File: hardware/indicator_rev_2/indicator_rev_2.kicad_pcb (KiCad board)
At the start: 2 copper layers, 55 x 56 mm, 28 parts, among them J2 Conn_01x04_Pin, U1 TCA6408ARSVR, U2 TLV70033DCKR

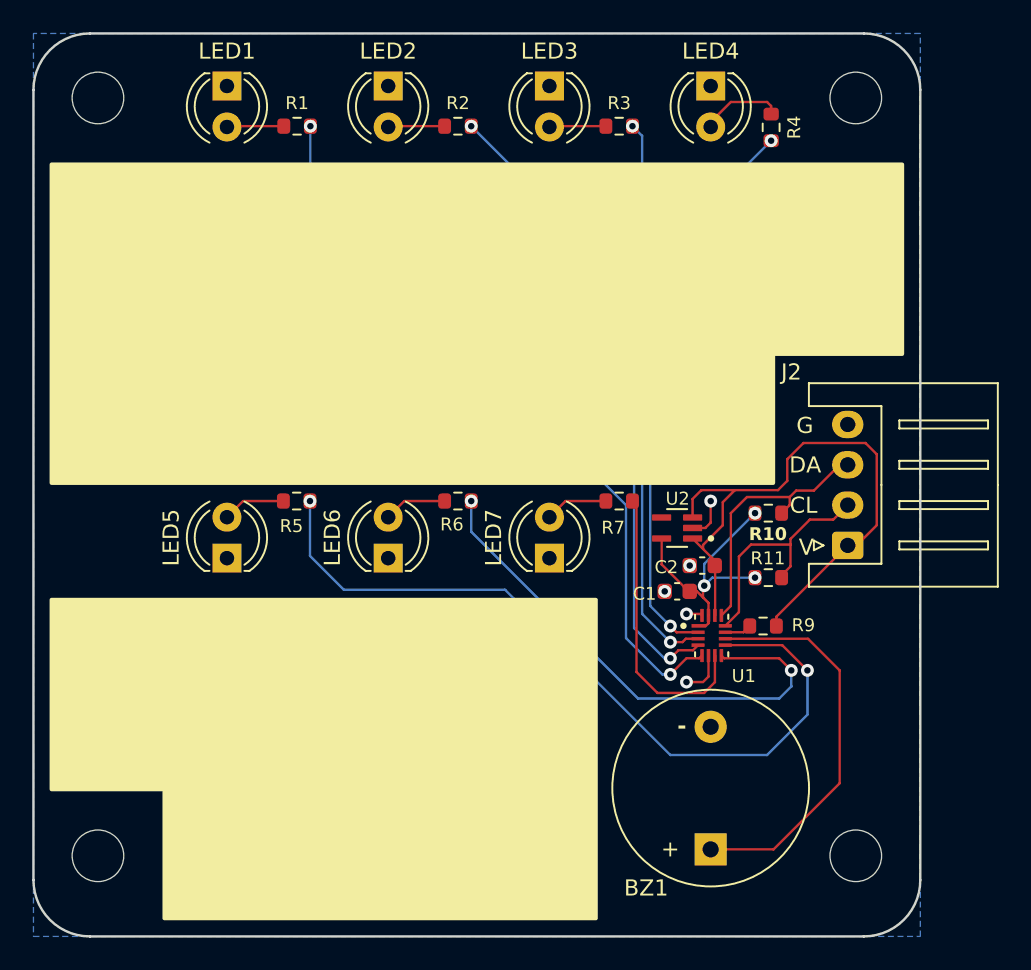
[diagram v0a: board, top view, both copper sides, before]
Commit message: modified i2c header and pushed connector
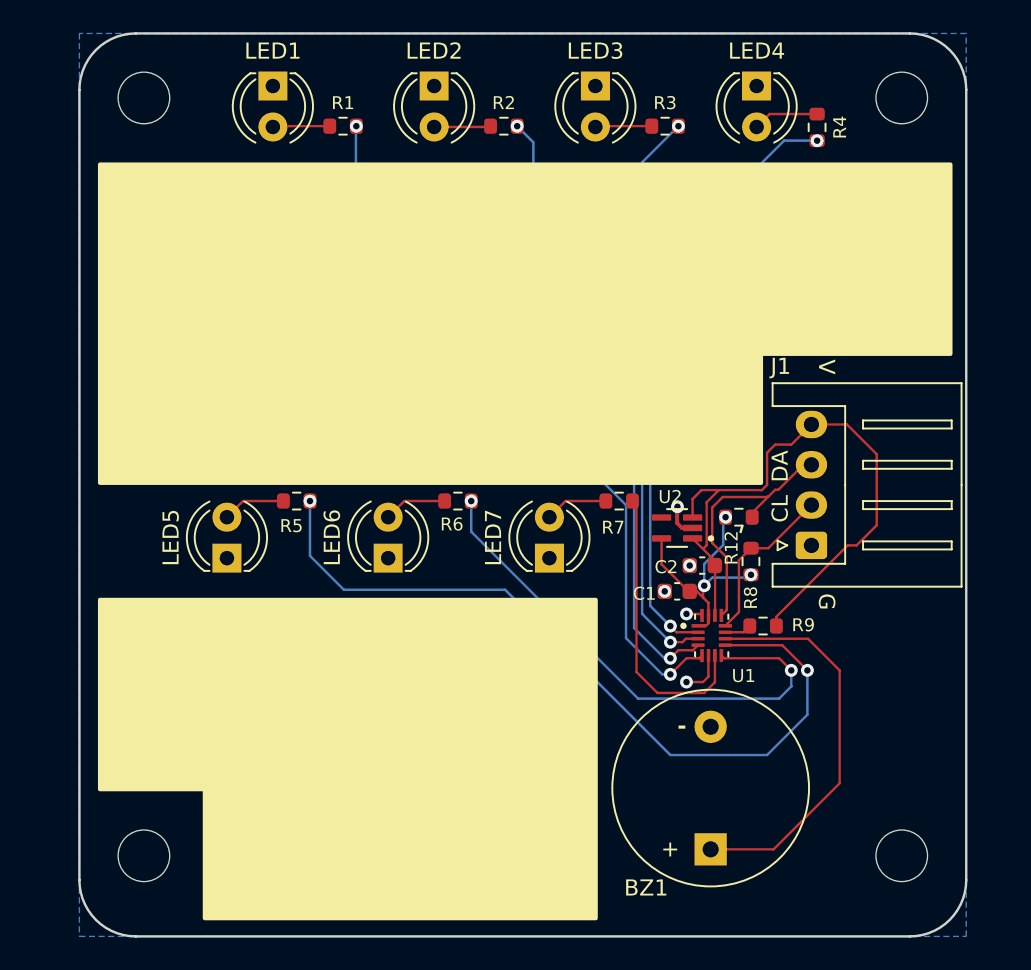
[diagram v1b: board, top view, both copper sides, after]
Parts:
- removed J2: Conn_01x04_Pin, Connector_JST:JST_XH_S4B-XH-A_1x04_P2.50mm_Horizontal
- removed R10, R11: 10k, Resistor_SMD:R_0603_1608Metric
- added J1: Conn_01x04, Connector_JST:JST_XH_S4B-XH-A_1x04_P2.50mm_Horizontal, F.Cu at (147.2, 114.8)
- added R12: 10k, Resistor_SMD:R_0603_1608Metric, F.Cu at (142.8, 113.0)
- added R8: 10k, Resistor_SMD:R_0603_1608Metric, F.Cu at (143.5, 115.8)
- moved R3 2.85 mm to (138.2, 88.8)
- moved R1 2.85 mm to (118.2, 88.8)
- moved R2 2.85 mm to (128.2, 88.8)
- moved LED1 2.85 mm to (113.8, 86.3)
- moved LED2 2.85 mm to (123.8, 86.3)
- moved LED3 2.85 mm to (133.8, 86.3)
- moved LED4 2.85 mm to (143.8, 86.3)
- moved R4 2.85 mm to (147.6, 88.8)
- moved REF** 2.85 mm to (152.8, 134.0)
- moved REF** 2.85 mm to (152.8, 87.0)
- moved REF** 2.85 mm to (105.8, 87.0)
- moved REF** 2.85 mm to (105.8, 134.0)
- moved G*** 0.99 mm to (119.0, 128.9)
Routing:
- net SCL: track 15.2 -> 10.3 mm
- net LED4: track 35.6 -> 38.0 mm
- net +3V3: track 16.9 -> 15.7 mm
- net LED2: track 40.6 -> 39.4 mm
- net LED1: track 46.0 -> 44.8 mm
- net Net-(LED4-A): track 5.17 -> 4.08 mm
- net +5V: track 38.5 -> 39.4 mm
- net LED3: track 34.8 -> 35.5 mm

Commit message: added b. silkscreen text & modified board colours
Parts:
- moved G*** 2.42 mm to (119.0, 126.5)
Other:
- board text added: "Indicator Board"
- board text added: "Rev. 2.0"
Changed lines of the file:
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@@
 	)
 	(setup
+		(stackup
+			(layer "F.SilkS"
+				(type "Top Silk Screen")
+				(color "White")
+			)
+			(layer "F.Paste"
+				(type "Top Solder Paste")
+			)
+			(layer "F.Mask"
+				(type "Top Solder Mask")
+				(color "Green")
+				(thickness 0.01)
+			)
+			(layer "F.Cu"
+				(type "copper")
+				(thickness 0.035)
+			)
+			(layer "dielectric 1"
+				(type "core")
+				(color "FR4 natural")
+				(thickness 1.51)
+				(material "FR4")
+				(epsilon_r 4.5)
+				(loss_tangent 0.02)
+			)
+			(layer "B.Cu"
+				(type "copper")
+				(thickness 0.035)
+			)
+			(layer "B.Mask"
+				(type "Bottom Solder Mask")
+				(color "Green")
+				(thickness 0.01)
+			)
+			(layer "B.Paste"
+				(type "Bottom Solder Paste")
+			)
+			(layer "B.SilkS"
+				(type "Bottom Silk Screen")
+				(color "White")
+			)
+			(copper_finish "None")
+			(dielectric_constraints no)
+		)
 		(pad_to_mask_clearance 0)
 		(allow_soldermask_bridges_in_footprints no)
@@
 	(footprint "Symbol:HPVDT-Logo_1526.1x139.6mm_SilkScreen"
 		(layer "B.Cu")
-		(at 119 128.917 180)
+		(at 119 126.5 180)
 		(property "Reference" "G***"
 			(at 0 0 0)
@@
 		(layer "F.SilkS")
 	)
+	(gr_rect
+		(start 111.1 129.4)
+		(end 115.1 133.4)
+		(stroke
+			(width 0.15)
+			(type solid)
+		)
+		(fill yes)
+		(layer "B.SilkS")
+	)
+	(gr_rect
+		(start 110.6 128.9)
+		(end 115.6 133.9)
+		(stroke
+			(width 0.15)
+			(type default)
+		)
+		(fill no)
+		(layer "B.SilkS")
+	)
 	(gr_line
 		(start 153.35 139)
@@
 		)
 	)
+	(gr_text "Rev. 2.0"
+		(at 125.9 133.6 0)
+		(layer "B.SilkS")
+		(effects
+			(font
+				(size 1.5 1.5)
+				(thickness 0.3)
+				(bold yes)
+			)
+			(justify left bottom mirror)
+		)
+	)
 	(gr_text "CL"
 		(at 145.9 111.2355 90)
@@
 	)
 	(gr_text "Abdullah Alsafar"
-		(at 134.494 126.25 0)
+		(at 128.538154 123.9 0)
 		(layer "B.SilkS")
 		(effects
@@
 		)
 	)
+	(gr_text "Indicator Board"
+		(at 134.2 130.9 0)
+		(layer "B.SilkS")
+		(effects
+			(font
+				(size 1.5 1.5)
+				(thickness 0.3)
+				(bold yes)
+			)
+			(justify left bottom mirror)
+		)
+	)
